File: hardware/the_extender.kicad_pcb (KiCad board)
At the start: 4 copper layers, 51.2 x 50.9 mm, 119 parts, among them J0 U262-241N-4BV60, J1 USB_C_Receptacle_USB2.0, J2 U231-091N-3BLRC11, J3 PJ-3136-B, J4 PJ-3136-B, J5 AF 10.0 HC6.3, Q1 SSM3J332R,LF, Q2 SSM3J332R,LF, Q3 Q_PNP_CBE, Q4 SSM3J332R,LF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

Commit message: fix bugs
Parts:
- moved TP1 2.33 mm to (92.2, 36.1)
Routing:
- net CHG_CC1: track 35.0 -> 25.6 mm
- net +3V3: track 114.9 -> 113.0 mm
- net GND: vias 154 -> 169

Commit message: fix bugs
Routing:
- net GND: track 203.3 -> 185.6 mm

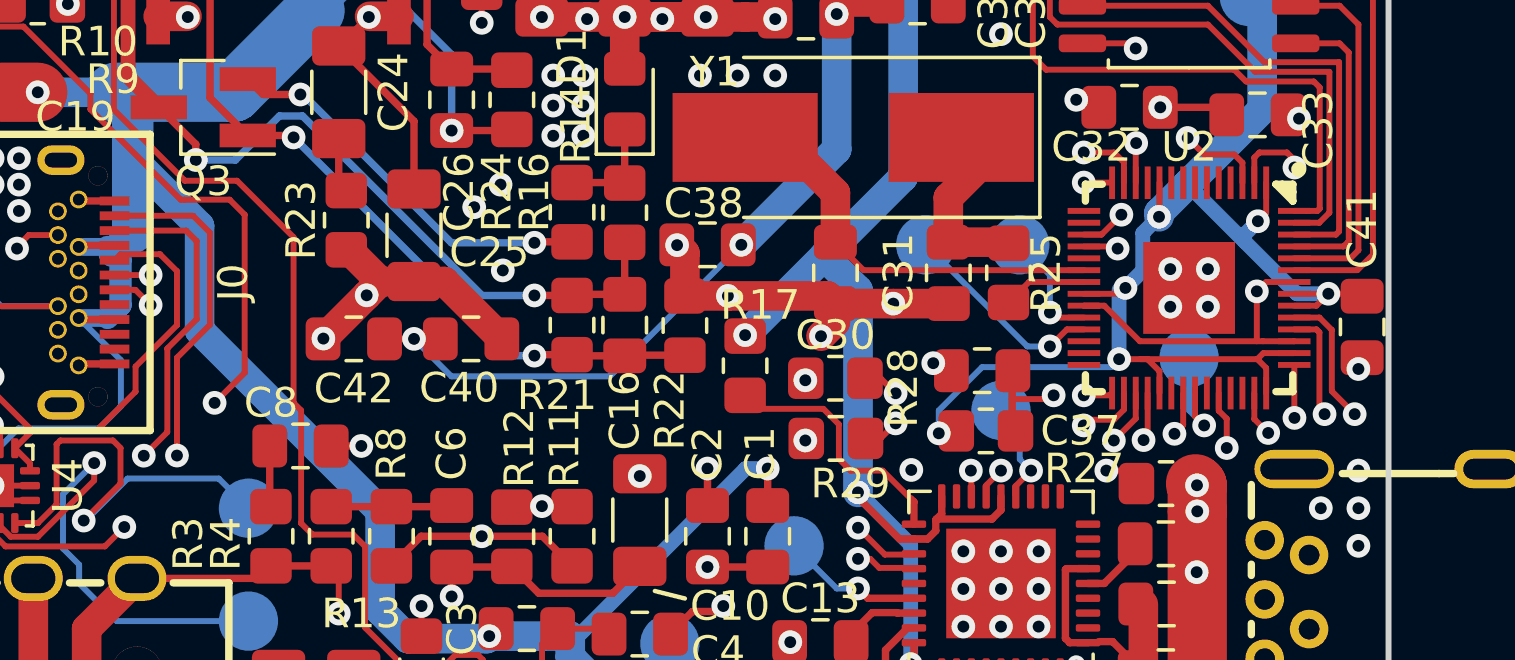
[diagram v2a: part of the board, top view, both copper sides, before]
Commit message: add missing trace, fix bugs
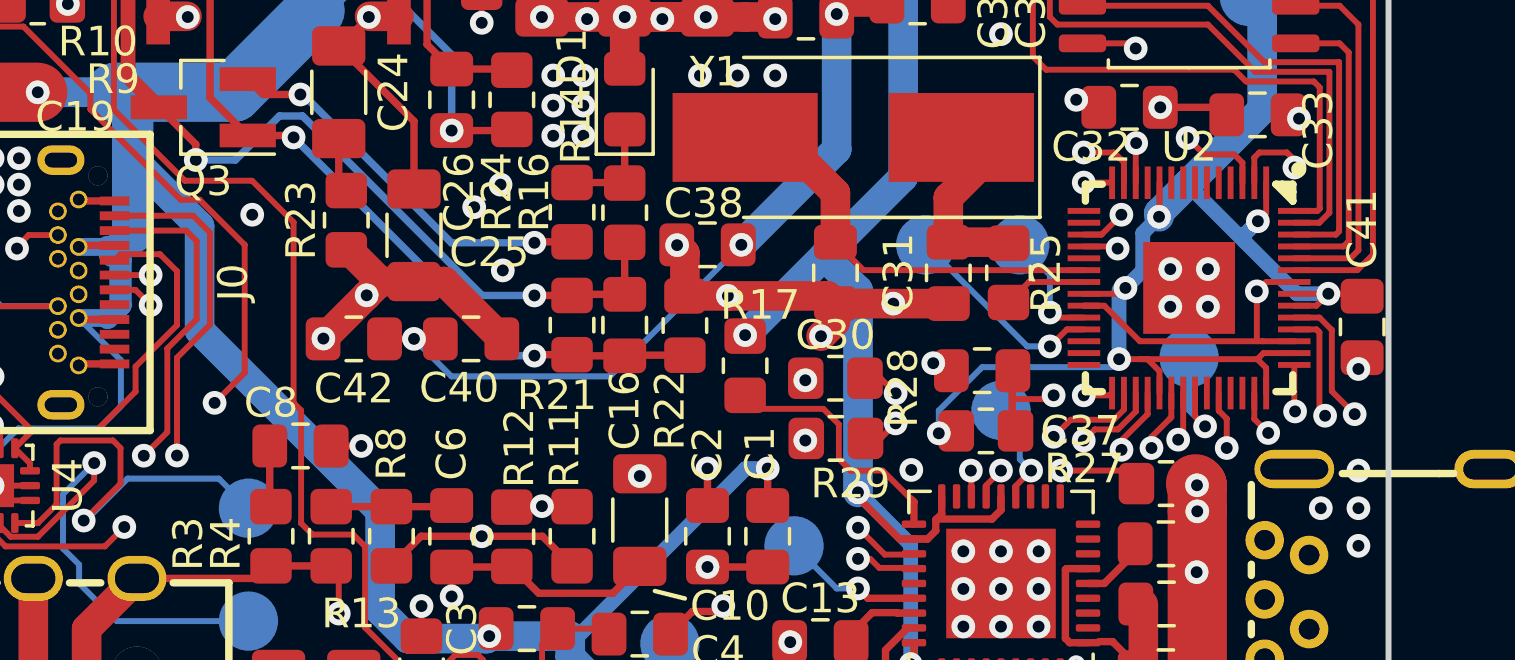
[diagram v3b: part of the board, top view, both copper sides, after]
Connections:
- U2 pad 34: unconnected-(U2-Pad34) -> SND_MIC_EN
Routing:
- net SND_MIC_EN: track 4.02 -> 32.7 mm, vias 1 -> 2
- net SND_EEPROM_SCK: track 29.8 -> 28.8 mm
- net Net-(D2-Pad4): track 31.5 -> 30.9 mm
- net GND: vias 169 -> 170

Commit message: added even more connections i forgot
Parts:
- moved R32 0.45 mm to (91.7, 30.1)
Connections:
- U2 pad 3: HUB_EN -> unconnected-(U2-Pad3)
- U2 pad 6: unconnected-(U2-Pad6) -> HUB_EN
- U2 pad 7: unconnected-(U2-Pad7) -> REG3_PS
- U5 pad 26: unconnected-(U5-Pad26) -> +3.3VP
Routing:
- net REG3_PS: track 0.00 -> 23.7 mm, vias 0 -> 2
- net HUB_EN: track 12.7 -> 11.6 mm
- net +3.3VP: track 62.2 -> 63.0 mm
- net +5V: track 163.7 -> 164.4 mm, vias 9 -> 10
- net +1V1: track 21.0 -> 21.5 mm
- net GND: track 185.6 -> 186.0 mm, vias 170 -> 178

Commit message: stuff
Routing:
- net Net-(C10-Pad1): track 24.1 -> 26.4 mm
- net SND_L: track 16.0 -> 16.6 mm
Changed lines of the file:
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@@
   (segment (start 69.215 69.4) (end 69.33 69.285) (width 0.25) (layer "F.Cu") (net 5))
   (segment (start 69.33 69.285) (end 69.33 67.75) (width 0.25) (layer "F.Cu") (net 5))
-  (segment (start 61.976 60.052) (end 61.976 58.782) (width 0.25) (layer "F.Cu") (net 5))
+  (segment (start 61.976 60.052) (end 61.976 58.782) (width 1) (layer "F.Cu") (net 5))
   (via (at 61.976 60.052) (size 0.8) (drill 0.4) (layers "F.Cu" "B.Cu") (free) (net 5))
   (via (at 69.215 69.4) (size 0.8) (drill 0.4) (layers "F.Cu" "B.Cu") (free) (net 5))
-  (segment (start 67.116386 67.691) (end 68.58 67.691) (width 0.25) (layer "In1.Cu") (net 5))
-  (segment (start 61.976 60.052) (end 61.976 62.550614) (width 0.25) (layer "In1.Cu") (net 5))
-  (segment (start 68.58 67.691) (end 69.215 68.326) (width 0.25) (layer "In1.Cu") (net 5))
-  (segment (start 69.215 68.326) (end 69.215 69.4) (width 0.25) (layer "In1.Cu") (net 5))
-  (segment (start 61.976 62.550614) (end 67.116386 67.691) (width 0.25) (layer "In1.Cu") (net 5))
-  (segment (start 61.976 61.907) (end 61.976 63.939) (width 0.25) (layer "F.Cu") (net 6))
-  (segment (start 61.976 63.939) (end 61.214 64.701) (width 0.25) (layer "F.Cu") (net 6))
+  (segment (start 68.072 68.199) (end 69.215 69.342) (width 0.5) (layer "In1.Cu") (net 5))
+  (segment (start 66.929 68.199) (end 68.072 68.199) (width 0.5) (layer "In1.Cu") (net 5))
+  (segment (start 61.976 60.052) (end 61.976 63.246) (width 0.5) (layer "In1.Cu") (net 5))
+  (segment (start 61.976 63.246) (end 66.929 68.199) (width 0.5) (layer "In1.Cu") (net 5))
+  (segment (start 69.215 69.342) (end 69.215 69.4) (width 0.5) (layer "In1.Cu") (net 5))
+  (segment (start 61.976 61.907) (end 61.976 63.939) (width 1) (layer "F.Cu") (net 6))
+  (segment (start 61.976 63.939) (end 61.214 64.701) (width 1) (layer "F.Cu") (net 6))
   (segment (start 63.5 72.11) (end 64.5408 71.0692) (width 0.7) (layer "F.Cu") (net 7))
-  (segment (start 65.278 55.3245) (end 67.2885 55.3245) (width 0.25) (layer "F.Cu") (net 7))
+  (segment (start 70.67 56.261) (end 68.268 56.261) (width 0.5) (layer "F.Cu") (net 7))
+  (segment (start 65.278 55.3245) (end 67.2885 55.3245) (width 0.5) (layer "F.Cu") (net 7))
   (segment (start 66.905512 70.96348) (end 68.47848 70.96348) (width 0.7) (layer "F.Cu") (net 7))
   (segment (start 65.83 65.8) (end 65.83 67.75) (width 0.25) (layer "F.Cu") (net 7))
-  (segment (start 67.2885 55.3245) (end 67.31 55.303) (width 0.25) (layer "F.Cu") (net 7))
+  (segment (start 67.2885 55.3245) (end 67.31 55.303) (width 1) (layer "F.Cu") (net 7))
   (segment (start 47.958 62.009) (end 47.912 62.009) (width 1) (layer "F.Cu") (net 7))
   (segment (start 47.912 62.009) (end 46.958479 61.055479) (width 1) (layer "F.Cu") (net 7))
   (segment (start 68.7 71.185) (end 68.7 72.575) (width 0.5) (layer "F.Cu") (net 7))
   (segment (start 60.96 72.11) (end 63.5 72.11) (width 1) (layer "F.Cu") (net 7))
-  (segment (start 68.21852 56.21152) (end 67.31 55.303) (width 0.25) (layer "F.Cu") (net 7))
   (segment (start 49.322 73.025) (end 60.045 73.025) (width 0.75) (layer "F.Cu") (net 7))
   (segment (start 69.83 67.75) (end 69.83 68.745) (width 0.25) (layer "F.Cu") (net 7))
@@
   (segment (start 46.958479 66.360521) (end 46.958479 70.661479) (width 1) (layer "F.Cu") (net 7))
   (segment (start 47.958 71.661) (end 49.322 73.025) (width 0.75) (layer "F.Cu") (net 7))
-  (segment (start 71.628 55.303) (end 70.71948 56.21152) (width 0.25) (layer "F.Cu") (net 7))
   (segment (start 47.958 65.361) (end 47.958 62.009) (width 1) (layer "F.Cu") (net 7))
   (segment (start 66.04 65.59) (end 65.83 65.8) (width 0.25) (layer "F.Cu") (net 7))
@@
   (segment (start 64.5408 71.0692) (end 66.799792 71.0692) (width 0.7) (layer "F.Cu") (net 7))
   (segment (start 47.958 65.361) (end 46.958479 66.360521) (width 1) (layer "F.Cu") (net 7))
+  (segment (start 71.628 55.303) (end 70.67 56.261) (width 0.5) (layer "F.Cu") (net 7))
   (segment (start 46.958479 70.661479) (end 47.958 71.661) (width 1) (layer "F.Cu") (net 7))
+  (segment (start 68.268 56.261) (end 67.31 55.303) (width 0.5) (layer "F.Cu") (net 7))
   (segment (start 46.958479 61.055479) (end 46.958479 56.708521) (width 1) (layer "F.Cu") (net 7))
   (segment (start 60.045 73.025) (end 60.96 72.11) (width 0.75) (layer "F.Cu") (net 7))
   (segment (start 66.799792 71.0692) (end 66.905512 70.96348) (width 0.7) (layer "F.Cu") (net 7))
   (segment (start 65.278 56.319) (end 65.278 55.3245) (width 0.25) (layer "F.Cu") (net 7))
-  (segment (start 70.71948 56.21152) (end 68.21852 56.21152) (width 0.25) (layer "F.Cu") (net 7))
   (via (at 65.278 56.319) (size 0.8) (drill 0.4) (layers "F.Cu" "B.Cu") (free) (net 7))
   (via (at 66.04 65.59) (size 0.8) (drill 0.4) (layers "F.Cu" "B.Cu") (free) (net 7))
@@
   (segment (start 61.214 53.287) (end 63.246 53.287) (width 0.25) (layer "F.Cu") (net 8))
   (segment (start 63.246 53.287) (end 65.2405 53.287) (width 0.25) (layer "F.Cu") (net 8))
-  (segment (start 59.436 60.052) (end 59.436 58.782) (width 0.25) (layer "F.Cu") (net 9))
+  (segment (start 59.436 60.052) (end 59.436 58.782) (width 1) (layer "F.Cu") (net 9))
   (segment (start 68.33 69.039458) (end 68.33 67.75) (width 0.25) (layer "F.Cu") (net 9))
   (segment (start 67.957229 69.412229) (end 68.33 69.039458) (width 0.25) (layer "F.Cu") (net 9))
   (via (at 67.957229 69.412229) (size 0.8) (drill 0.4) (layers "F.Cu" "B.Cu") (free) (net 9))
   (via (at 59.436 60.052) (size 0.8) (drill 0.4) (layers "F.Cu" "B.Cu") (free) (net 9))
-  (segment (start 67.957229 69.354229) (end 67.957229 69.412229) (width 0.25) (layer "In1.Cu") (net 9))
-  (segment (start 59.436 60.833) (end 67.957229 69.354229) (width 0.25) (layer "In1.Cu") (net 9))
-  (segment (start 59.436 60.052) (end 59.436 60.833) (width 0.25) (layer "In1.Cu") (net 9))
-  (segment (start 59.436 64.463) (end 59.182 64.717) (width 0.25) (layer "F.Cu") (net 10))
-  (segment (start 59.436 61.907) (end 59.436 64.463) (width 0.25) (layer "F.Cu") (net 10))
+  (segment (start 59.436 60.052) (end 59.436 61.976) (width 0.5) (layer "In1.Cu") (net 9))
+  (segment (start 59.436 61.976) (end 66.872229 69.412229) (width 0.5) (layer "In1.Cu") (net 9))
+  (segment (start 66.872229 69.412229) (end 67.957229 69.412229) (width 0.5) (layer "In1.Cu") (net 9))
+  (segment (start 59.436 64.463) (end 59.182 64.717) (width 1) (layer "F.Cu") (net 10))
+  (segment (start 59.436 61.907) (end 59.436 64.463) (width 1) (layer "F.Cu") (net 10))
   (segment (start 59.139 51.239) (end 59.139 53.244) (width 0.25) (layer "F.Cu") (net 11))
   (segment (start 59.139 53.244) (end 59.182 53.287) (width 0.25) (layer "F.Cu") (net 11))
@@
   (via (at 71.628 52.255) (size 0.8) (drill 0.4) (layers "F.Cu" "B.Cu") (net 13))
   (via (at 64.135 68.384) (size 0.8) (drill 0.4) (layers "F.Cu" "B.Cu") (net 13))
-  (segment (start 64.135 68.384) (end 65.540614 68.384) (width 0.25) (layer "In2.Cu") (net 13))
-  (segment (start 71.628 62.296614) (end 71.628 52.255) (width 0.25) (layer "In2.Cu") (net 13))
-  (segment (start 65.540614 68.384) (end 71.628 62.296614) (width 0.25) (layer "In2.Cu") (net 13))
+  (segment (start 70.231 67.31) (end 67.564 67.31) (width 1) (layer "In2.Cu") (net 13))
+  (segment (start 71.628 52.255) (end 71.882 52.509) (width 1) (layer "In2.Cu") (net 13))
+  (segment (start 71.882 52.509) (end 71.882 65.659) (width 1) (layer "In2.Cu") (net 13))
+  (segment (start 66.49 68.384) (end 64.135 68.384) (width 1) (layer "In2.Cu") (net 13))
+  (segment (start 67.564 67.31) (end 66.49 68.384) (width 1) (layer "In2.Cu") (net 13))
+  (segment (start 71.882 65.659) (end 70.231 67.31) (width 1) (layer "In2.Cu") (net 13))
   (segment (start 79.473125 56.864489) (end 78.7615 57.576114) (width 0.25) (layer "F.Cu") (net 14))
   (segment (start 78.7615 57.576114) (end 78.7615 57.843) (width 0.25) (layer "F.Cu") (net 14))

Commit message: fix
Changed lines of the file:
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@@
   (segment (start 69.63042 62.77242) (end 69.088 62.23) (width 0.2) (layer "In1.Cu") (net 125))
   (segment (start 82.13458 53.88242) (end 81.82242 54.19458) (width 0.2) (layer "In1.Cu") (net 125))
+  (segment (start 48.514 37.084) (end 49.022 37.592) (width 0.2) (layer "F.Cu") (net 145))
   (segment (start 48.292 36.862) (end 48.514 37.084) (width 0.2) (layer "F.Cu") (net 145))
+  (segment (start 53.086 39.878) (end 56.134 42.926) (width 0.2) (layer "F.Cu") (net 145))
   (segment (start 47.4026 36.862) (end 48.292 36.862) (width 0.2) (layer "F.Cu") (net 145))
+  (segment (start 56.134 42.926) (end 56.769 42.926) (width 0.2) (layer "F.Cu") (net 145))
+  (segment (start 49.022 37.592) (end 51.689 37.592) (width 0.2) (layer "F.Cu") (net 145))
+  (segment (start 51.689 37.592) (end 53.086 38.989) (width 0.2) (layer "F.Cu") (net 145))
+  (segment (start 64.262 56.642) (end 64.262 57.658) (width 0.2) (layer "F.Cu") (net 145))
   (segment (start 58.293 44.45) (end 58.293 48.768) (width 0.2) (layer "F.Cu") (net 145))
-  (segment (start 53.086 39.344439) (end 53.086 39.878) (width 0.2) (layer "F.Cu") (net 145))
-  (segment (start 56.134 42.926) (end 56.769 42.926) (width 0.2) (layer "F.Cu") (net 145))
-  (segment (start 64.262 56.642) (end 64.262 57.658) (width 0.2) (layer "F.Cu") (net 145))
-  (segment (start 50.825561 37.084) (end 53.086 39.344439) (width 0.2) (layer "F.Cu") (net 145))
-  (segment (start 48.514 37.084) (end 50.825561 37.084) (width 0.2) (layer "F.Cu") (net 145))
+  (segment (start 53.086 38.989) (end 53.086 39.878) (width 0.2) (layer "F.Cu") (net 145))
   (segment (start 58.293 48.768) (end 57.277 49.784) (width 0.2) (layer "F.Cu") (net 145))
-  (segment (start 53.086 39.878) (end 56.134 42.926) (width 0.2) (layer "F.Cu") (net 145))
   (segment (start 56.769 42.926) (end 58.293 44.45) (width 0.2) (layer "F.Cu") (net 145))
   (via (at 48.514 37.084) (size 0.8) (drill 0.4) (layers "F.Cu" "B.Cu") (free) (net 145))

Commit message: automatic cleanup
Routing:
- net GND: track 186.0 -> 168.8 mm
- net SND_LED_O: track 38.4 -> 34.9 mm, vias 1 -> 0
- net +BATT: track 125.6 -> 122.2 mm, vias 8 -> 6
- net +3V3: track 113.0 -> 110.8 mm
- net Net-(R33-Pad1): track 7.66 -> 6.61 mm
- net Net-(C37-Pad1): track 14.5 -> 13.4 mm
- net MIC_T: track 61.2 -> 60.3 mm
- net Net-(R19-Pad1): track 17.5 -> 16.7 mm
- net SND_EEPROM_DR: track 25.4 -> 24.7 mm
- net Net-(R17-Pad1): track 8.62 -> 7.98 mm
- net SND_EEPROM_DW: track 25.9 -> 25.3 mm
- net Net-(J3-PadT): track 15.7 -> 15.2 mm
- net Net-(C24-Pad1): track 27.7 -> 27.1 mm
- net Net-(D2-Pad4): vias 3 -> 2
